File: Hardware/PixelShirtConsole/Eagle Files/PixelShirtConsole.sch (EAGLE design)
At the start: 7 parts

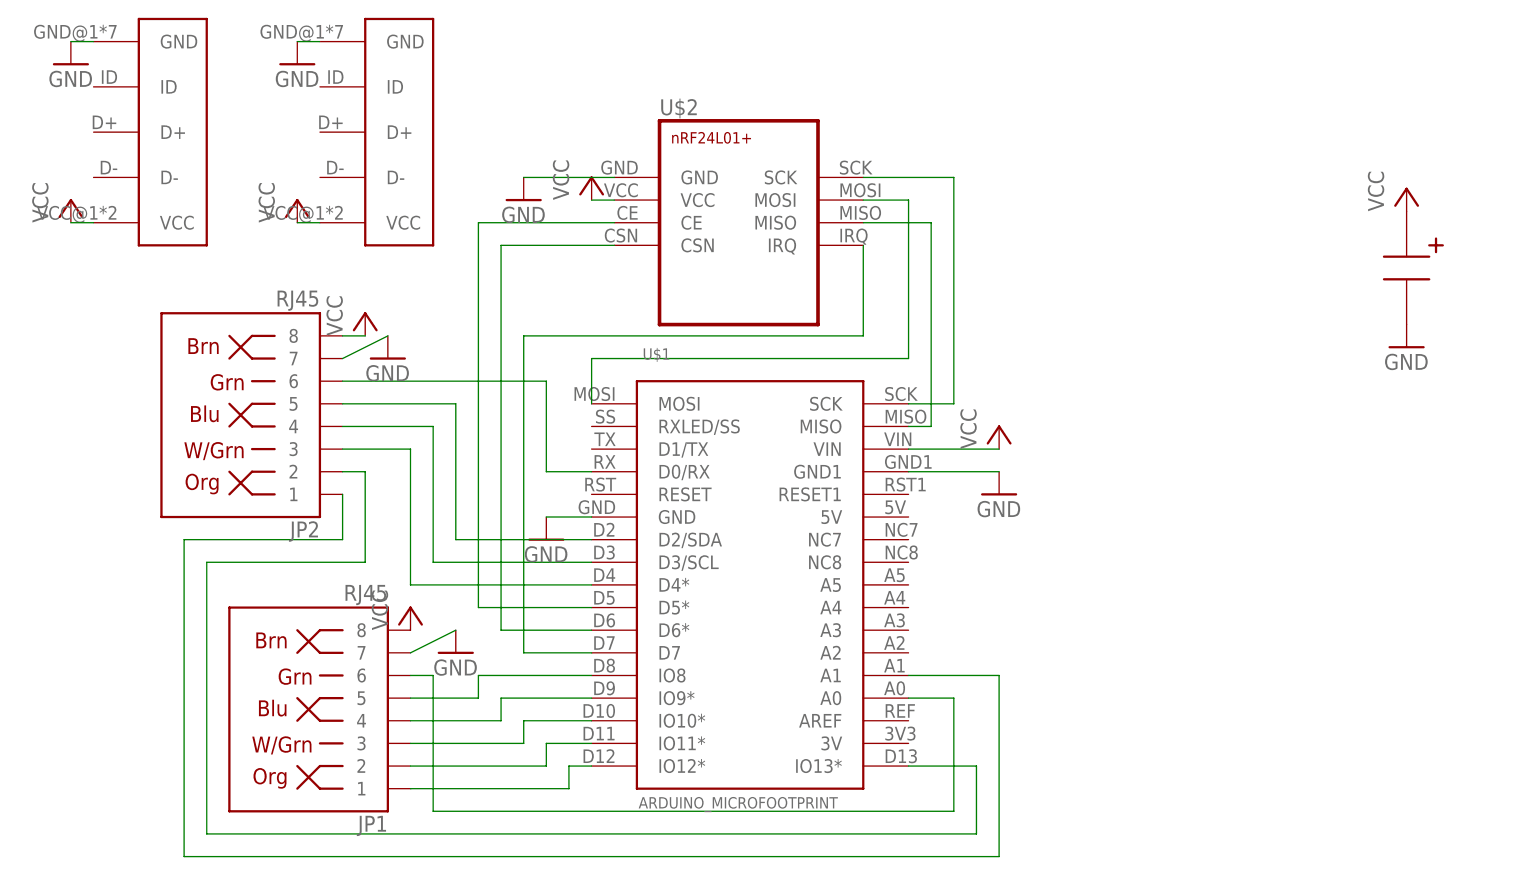
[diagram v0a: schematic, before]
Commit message: Moved some parts around for clearance Added logo, name Added Gerber files
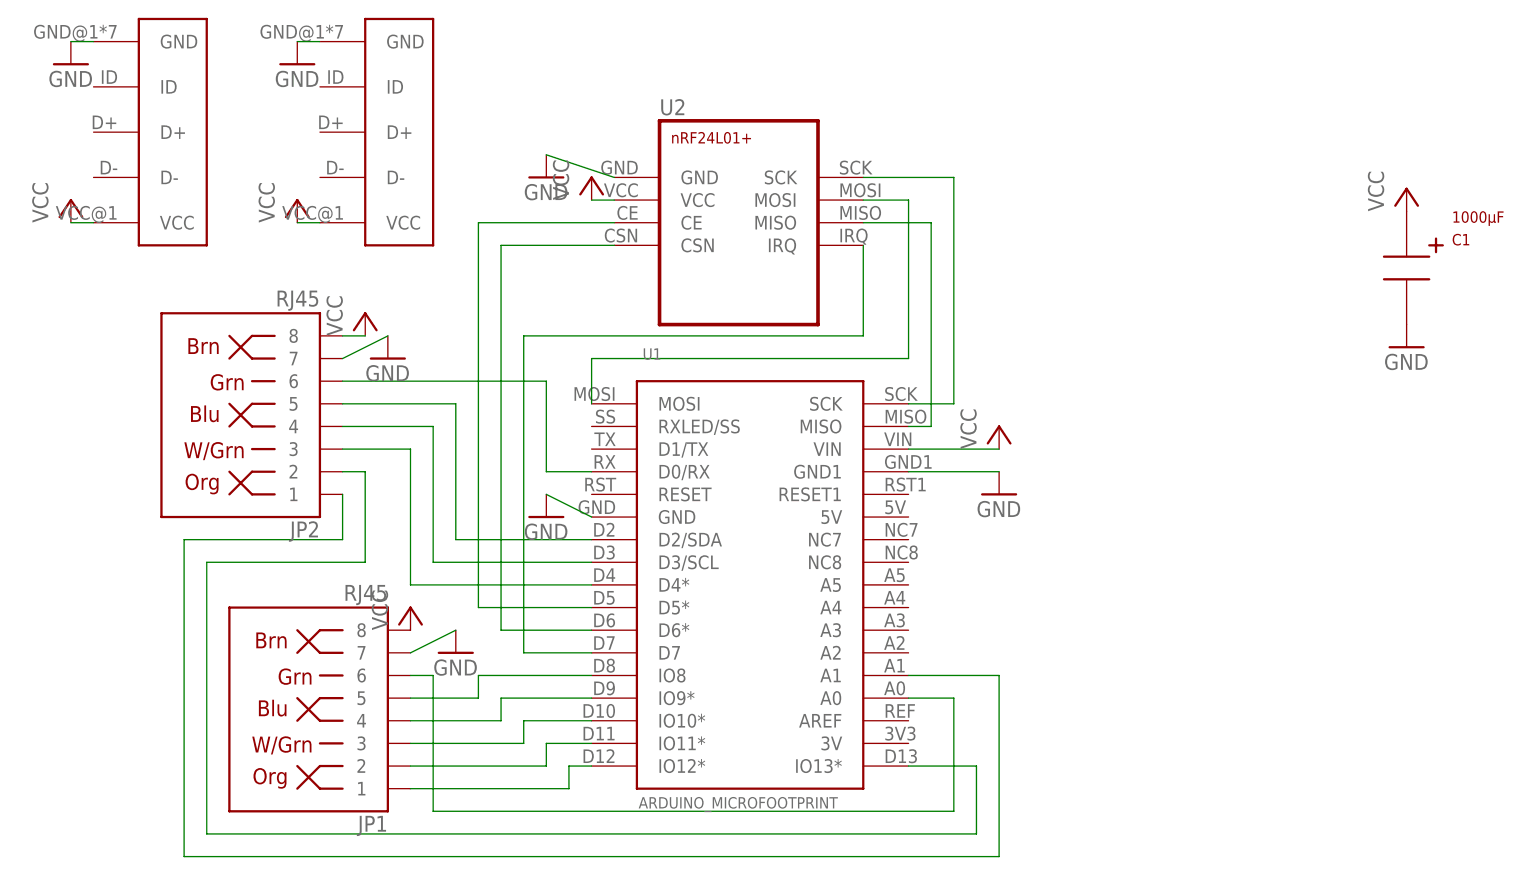
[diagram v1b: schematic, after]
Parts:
- C1: value CAP-CUSTOM -> 1000µF
- renumbered U$1 to U1, U$2 to U2, U$3 to JP4, U$4 to JP3

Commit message: Modified pin definitions for new board Fixed schematic issue where the nRF had 5V powering it instead of 3.3V
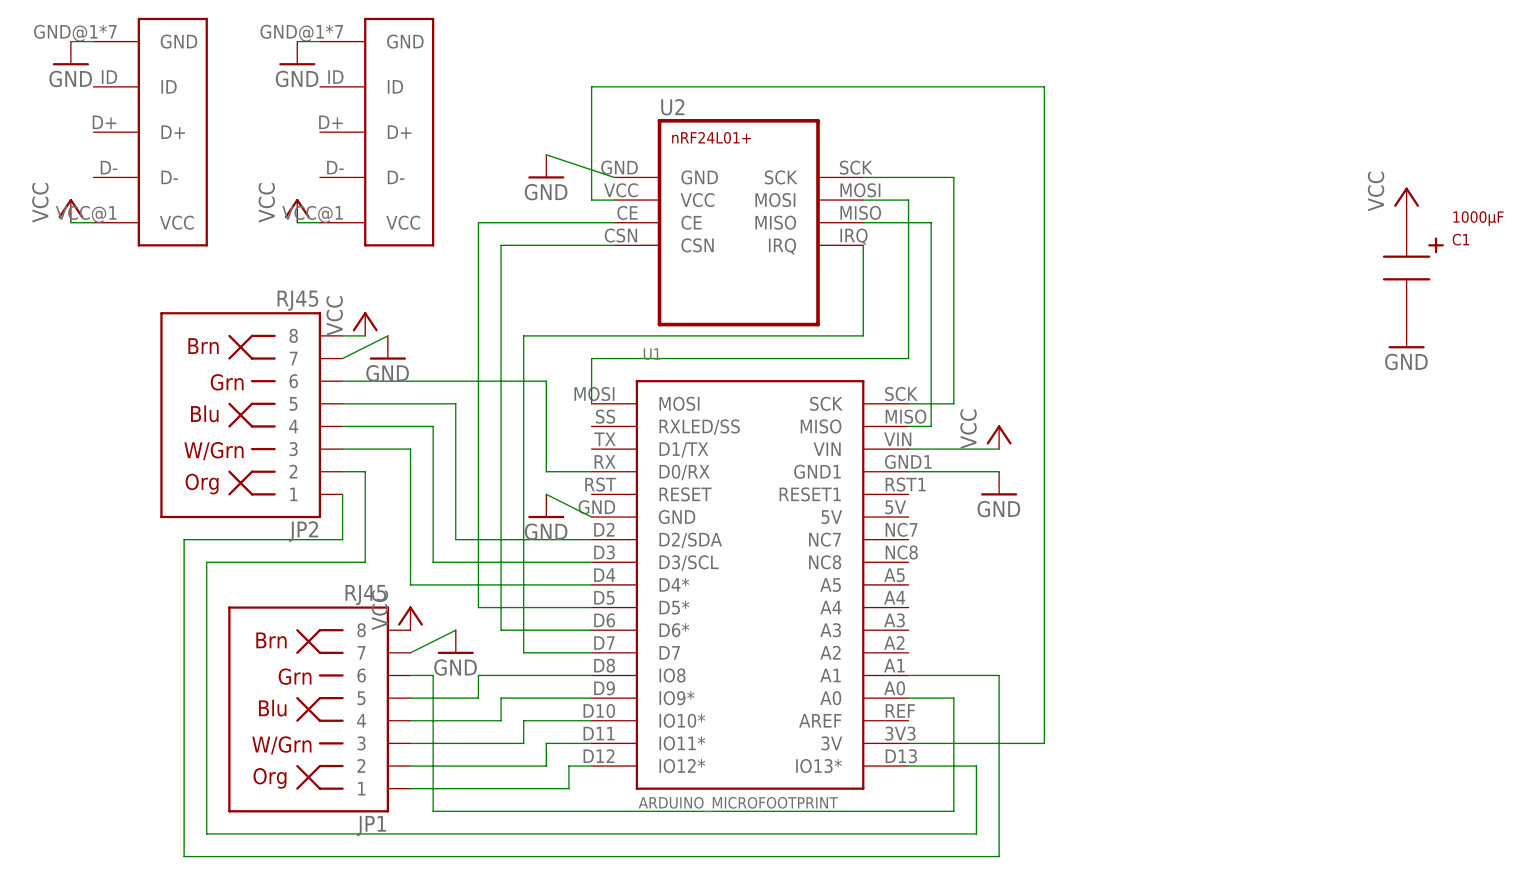
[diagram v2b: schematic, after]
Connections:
- new net N$19: U1.3V, U2.VCC
- net VCC: no longer U2.VCC
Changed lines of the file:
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@@
 <part name="GND3" library="supply1" deviceset="GND" device=""/>
 <part name="GND4" library="supply1" deviceset="GND" device=""/>
-<part name="P+4" library="supply1" deviceset="VCC" device=""/>
 <part name="GND5" library="supply1" deviceset="GND" device=""/>
 <part name="P+5" library="supply1" deviceset="VCC" device=""/>
@@
 <instance part="GND3" gate="1" x="81.28" y="66.04"/>
 <instance part="GND4" gate="1" x="81.28" y="104.14"/>
-<instance part="P+4" gate="VCC" x="86.36" y="104.14"/>
 <instance part="GND5" gate="1" x="71.12" y="50.8"/>
 <instance part="P+5" gate="VCC" x="66.04" y="55.88"/>
@@
 </segment>
 <segment>
-<pinref part="U2" gate="G$1" pin="VCC"/>
-<pinref part="P+4" gate="VCC" pin="VCC"/>
-<wire x1="86.36" y1="101.6" x2="88.9" y2="101.6" width="0.1524" layer="91"/>
-</segment>
-<segment>
 <pinref part="JP1" gate="JP1" pin="8"/>
 <pinref part="P+5" gate="VCC" pin="VCC"/>
@@
 </segment>
 </net>
+<net name="N$19" class="0">
+<segment>
+<pinref part="U2" gate="G$1" pin="VCC"/>
+<wire x1="88.9" y1="101.6" x2="86.36" y2="101.6" width="0.1524" layer="91"/>
+<wire x1="86.36" y1="101.6" x2="86.36" y2="114.3" width="0.1524" layer="91"/>
+<wire x1="86.36" y1="114.3" x2="137.16" y2="114.3" width="0.1524" layer="91"/>
+<wire x1="137.16" y1="114.3" x2="137.16" y2="40.64" width="0.1524" layer="91"/>
+<pinref part="U1" gate="G$1" pin="3V"/>
+<wire x1="137.16" y1="40.64" x2="121.92" y2="40.64" width="0.1524" layer="91"/>
+</segment>
+</net>
